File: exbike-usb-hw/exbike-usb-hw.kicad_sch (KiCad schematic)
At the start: 19 parts, among them J1 ICSP, J2 USB_B, J3 AudioJack3_SwitchTR, J4 J1, J5 J2, U1 ATtiny24A-SS, U2 AMS1117-3.3, Y1 12 MHz

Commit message: Layout
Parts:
- removed C5: 100nF, Capacitor_SMD:C_0805_2012Metric_Pad1.18x1.45mm_HandSolder, symbol Device:C
- removed J1: ICSP, Connector_PinHeader_2.54mm:PinHeader_1x06_P2.54mm_Vertical, symbol Connector_Generic:Conn_02x03_Counter_Clockwise
- removed J4: J1, Connector_PinHeader_2.54mm:PinHeader_1x02_P2.54mm_Vertical, symbol Connector:Conn_01x02_Pin
- removed J5: J2, Connector_PinHeader_2.54mm:PinHeader_1x02_P2.54mm_Vertical, symbol Connector:Conn_01x02_Pin
- added J1: ICSP, Connector_PinHeader_2.54mm:PinHeader_1x06_P2.54mm_Vertical, symbol Connector:Conn_01x06_Pin
- added TP2: TestPoint, TestPoint:TestPoint_Pad_D1.0mm, symbol Connector:TestPoint
- TP1: value CK -> TestPoint; footprint TestPoint:TestPoint_Pad_1.5x1.5mm -> TestPoint:TestPoint_Pad_D1.5mm
- Y1: footprint Crystal:Crystal_SMD_3225-4Pin_3.2x2.5mm -> Crystal:Crystal_HC49-4H_Vertical
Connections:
- net PA2 is gone; now on net +3V3: U1.11 (PA2)
- net +3V3: now also J1.3 (Pin_3)
- net GND: now also J1.6 (Pin_6)
- net MISO: now also J1.4 (Pin_4)
- net MOSI: now also J1.1 (Pin_1)
- net RST: now also J1.2 (Pin_2)
- net SCK: now also J1.5 (Pin_5)
- net at C1.1, U1.2 (XTAL1/PB0): now also Y1.2; no longer Y1.3
- net at U1.5 (PB2): now also TP2.1; no longer TP1.1
- net PA3: no longer names the net of U1.10 (PA3)
- net PA3: now also TP1.1
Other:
- moved on the sheet: C6

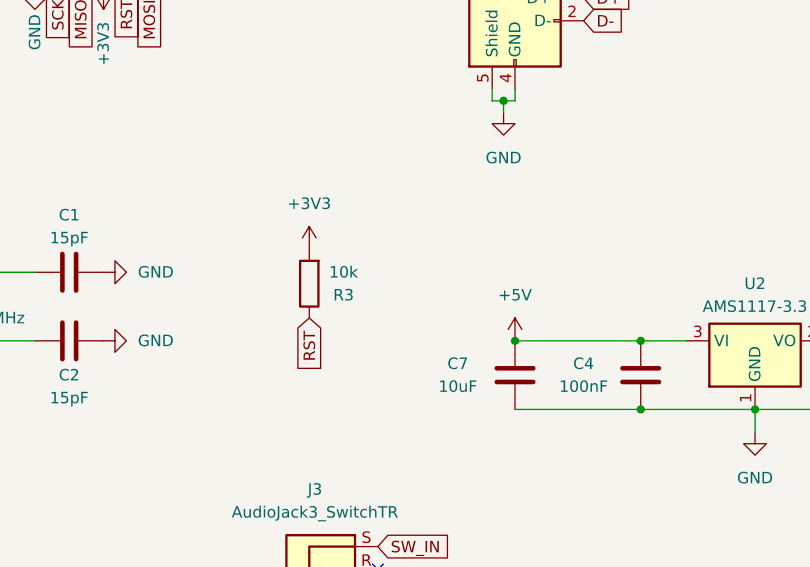
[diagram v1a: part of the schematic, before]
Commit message: Add d- pullup:
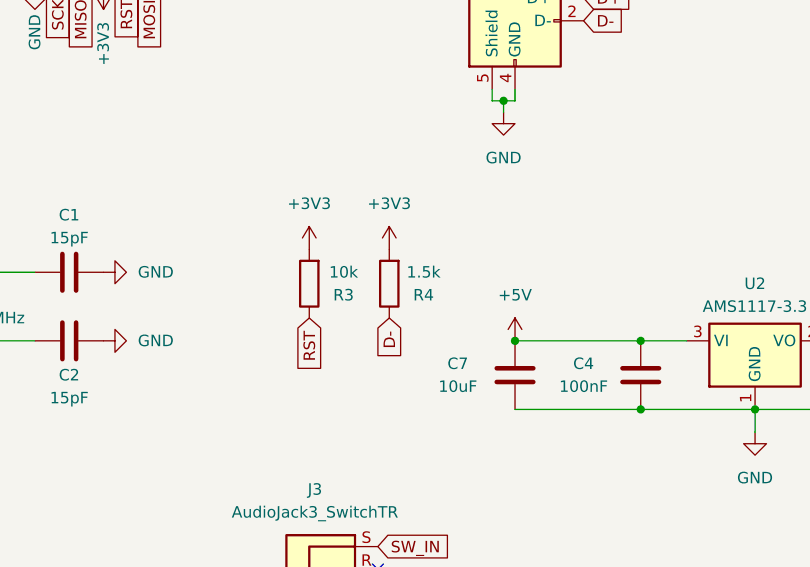
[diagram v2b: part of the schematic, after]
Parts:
- added R4: 1.5k, Resistor_SMD:R_0805_2012Metric_Pad1.20x1.40mm_HandSolder, symbol Device:R
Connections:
- net +3V3: now also R4.2
- net D-: now also R4.1
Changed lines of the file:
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@@
     (stroke (width 0) (type default))
+  )
+  (global_label "D-" (shape input) (at 147.32 63.5 270) (fields_autoplaced)
+    (effects (font (size 1.27 1.27)) (justify right))
+    (property "Intersheetrefs" "${INTERSHEET_REFS}" (at 147.32 69.2482 90)
+      (effects (font (size 1.27 1.27)) (justify right) hide)
+    )
   )
   (global_label "SW_IN" (shape input) (at 146.05 88.9 0) (fields_autoplaced)
@@
         (path "/bf0de29e-bdfb-4ae7-a755-5db6919b52b8"
           (reference "J1") (unit 1)
+        )
+      )
+    )
+  )
+  (symbol (lib_id "power:+3V3") (at 147.32 55.88 0) (unit 1)
+    (in_bom yes) (on_board yes) (dnp no) (fields_autoplaced)
+    (property "Reference" "#PWR017" (at 147.32 59.69 0)
+      (effects (font (size 1.27 1.27)) hide)
+    )
+    (property "Value" "+3V3" (at 147.32 50.8 0)
+      (effects (font (size 1.27 1.27)))
+    )
+    (property "Footprint" "" (at 147.32 55.88 0)
+      (effects (font (size 1.27 1.27)) hide)
+    )
+    (property "Datasheet" "" (at 147.32 55.88 0)
+      (effects (font (size 1.27 1.27)) hide)
+    )
+    (pin "1")
+    (instances
+      (project "exbike-usb-hw"
+        (path "/bf0de29e-bdfb-4ae7-a755-5db6919b52b8"
+          (reference "#PWR017") (unit 1)
         )
       )
@@
         )
       )
+    )
+  )
+  (symbol (lib_id "Device:R") (at 147.32 59.69 180) (unit 1)
+    (in_bom yes) (on_board yes) (dnp no)
+    (property "Reference" "R4" (at 151.13 60.96 0)
+      (effects (font (size 1.27 1.27)))
+    )
+    (property "Value" "1.5k" (at 151.13 58.42 0)
+      (effects (font (size 1.27 1.27)))
+    )
+    (property "Footprint" "Resistor_SMD:R_0805_2012Metric_Pad1.20x1.40mm_HandSolder" (at 149.098 59.69 90)
+      (effects (font (size 1.27 1.27)) hide)
+    )
+    (property "Datasheet" "~" (at 147.32 59.69 0)
+      (effects (font (size 1.27 1.27)) hide)
+    )
+    (pin "1")
+    (pin "2")
+    (instances
+      (project "exbike-usb-hw"
+        (path "/bf0de29e-bdfb-4ae7-a755-5db6919b52b8"
+          (reference "R4") (unit 1)
+        )
+      )

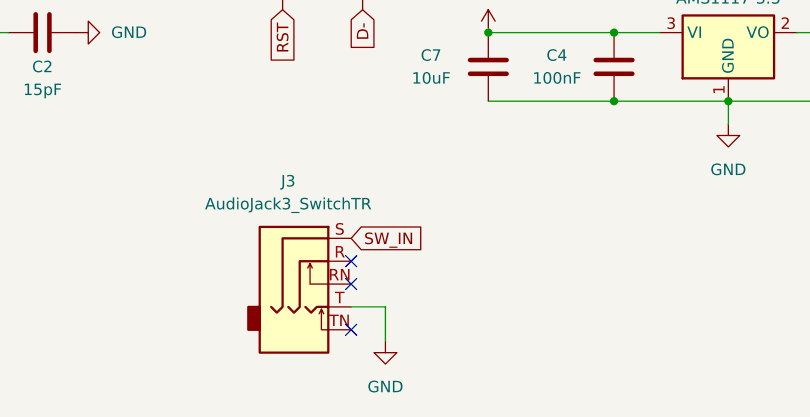
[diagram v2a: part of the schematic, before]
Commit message: Early USB code, PCB project cleanup
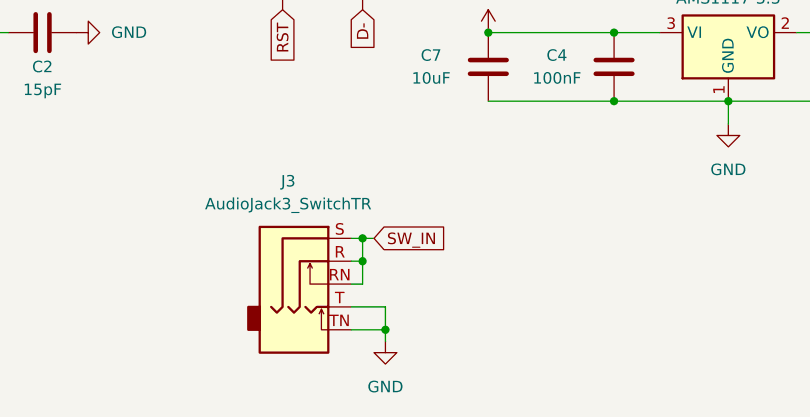
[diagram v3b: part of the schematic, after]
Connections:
- net GND: now also J3.TN
- net SW_IN: now also J3.R, J3.RN
- no-connect marks 3 -> 0
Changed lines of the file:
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@@
   (junction (at 175.26 73.66) (diameter 0) (color 0 0 0 0)
   )
+  (junction (at 147.32 88.9) (diameter 0) (color 0 0 0 0)
+  )
   (junction (at 175.26 66.04) (diameter 0) (color 0 0 0 0)
+  )
+  (junction (at 149.86 99.06) (diameter 0) (color 0 0 0 0)
   )
   (junction (at 201.93 66.04) (diameter 0) (color 0 0 0 0)
@@
   (junction (at 96.52 58.42) (diameter 0) (color 0 0 0 0)
   )
-  (no_connect (at 146.05 93.98))
-  (no_connect (at 146.05 99.06))
-  (no_connect (at 146.05 91.44))
+  (junction (at 147.32 91.44) (diameter 0) (color 0 0 0 0)
+  )
   (wire (pts (xy 158.75 38.1) (xy 158.75 39.37))
+    (stroke (width 0) (type default))
+  )
+  (wire (pts (xy 146.05 93.98) (xy 147.32 93.98))
     (stroke (width 0) (type default))
   )
@@
     (stroke (width 0) (type default))
   )
+  (wire (pts (xy 146.05 91.44) (xy 147.32 91.44))
+    (stroke (width 0) (type default))
+  )
   (wire (pts (xy 91.44 58.42) (xy 96.52 58.42))
     (stroke (width 0) (type default))
@@
   )
   (wire (pts (xy 175.26 66.04) (xy 180.34 66.04))
+    (stroke (width 0) (type default))
+  )
+  (wire (pts (xy 147.32 91.44) (xy 147.32 88.9))
     (stroke (width 0) (type default))
   )
@@
     (stroke (width 0) (type default))
   )
-  (wire (pts (xy 149.86 96.52) (xy 149.86 100.33))
+  (wire (pts (xy 149.86 96.52) (xy 149.86 99.06))
     (stroke (width 0) (type default))
   )
@@
     (stroke (width 0) (type default))
   )
+  (wire (pts (xy 148.59 88.9) (xy 147.32 88.9))
+    (stroke (width 0) (type default))
+  )
   (wire (pts (xy 74.93 40.64) (xy 81.28 40.64))
+    (stroke (width 0) (type default))
+  )
+  (wire (pts (xy 147.32 93.98) (xy 147.32 91.44))
     (stroke (width 0) (type default))
   )
@@
     (stroke (width 0) (type default))
   )
+  (wire (pts (xy 149.86 99.06) (xy 149.86 100.33))
+    (stroke (width 0) (type default))
+  )
   (wire (pts (xy 171.45 20.32) (xy 171.45 22.86))
     (stroke (width 0) (type default))
@@
   )
   (wire (pts (xy 161.29 66.04) (xy 175.26 66.04))
+    (stroke (width 0) (type default))
+  )
+  (wire (pts (xy 146.05 99.06) (xy 149.86 99.06))
+    (stroke (width 0) (type default))
+  )
+  (wire (pts (xy 147.32 88.9) (xy 146.05 88.9))
     (stroke (width 0) (type default))
   )
@@
     )
   )
-  (global_label "SW_IN" (shape input) (at 146.05 88.9 0) (fields_autoplaced)
+  (global_label "SW_IN" (shape input) (at 148.59 88.9 0) (fields_autoplaced)
     (effects (font (size 1.27 1.27)) (justify left))
-    (property "Intersheetrefs" "${INTERSHEET_REFS}" (at 154.5196 88.9 0)
+    (property "Intersheetrefs" "${INTERSHEET_REFS}" (at 157.0596 88.9 0)
       (effects (font (size 1.27 1.27)) (justify left) hide)
     )
